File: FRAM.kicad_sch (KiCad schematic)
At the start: 1 part

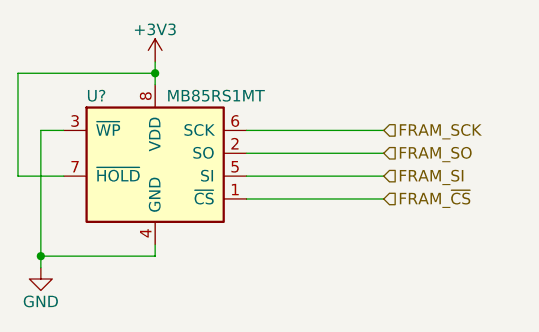
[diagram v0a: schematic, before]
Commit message: Fleshed out digital IO
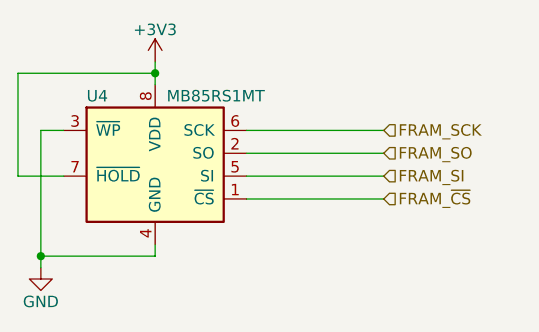
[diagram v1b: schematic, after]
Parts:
- gave numbers to parts that had none: 1
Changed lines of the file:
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@@
   (symbol (lib_id "Memory_NVRAM:MB85RS1MT") (at 129.54 76.2 0) (unit 1)
     (in_bom yes) (on_board yes)
-    (property "Reference" "U?" (id 0) (at 132.08 72.39 0)
+    (property "Reference" "U4" (id 0) (at 132.08 72.39 0)
       (effects (font (size 1.27 1.27)) (justify left))
     )
@@
   (symbol (lib_id "power:GND") (at 127 91.44 0) (unit 1)
     (in_bom yes) (on_board yes)
-    (property "Reference" "#PWR?" (id 0) (at 127 97.79 0)
+    (property "Reference" "#PWR011" (id 0) (at 127 97.79 0)
       (effects (font (size 1.27 1.27)) hide)
     )
@@
   (symbol (lib_id "power:+3V3") (at 139.7 68.58 0) (unit 1)
     (in_bom yes) (on_board yes)
-    (property "Reference" "#PWR?" (id 0) (at 139.7 72.39 0)
+    (property "Reference" "#PWR012" (id 0) (at 139.7 72.39 0)
       (effects (font (size 1.27 1.27)) hide)
     )
